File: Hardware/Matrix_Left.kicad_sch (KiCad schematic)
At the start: 125 parts, among them SW10 PG1350, SW11 PG1350, SW12 PG1350, SW13 PG1350, SW14 PG1350, SW15 PG1350, SW16 PG1350, SW17 PG1350, SW18 PG1350, SW19 PG1350, SW20 PG1350, SW21 PG1350, SW22 PG1350, SW23 PG1350, SW24 PG1350, SW25 PG1350, SW26 PG1350, SW27 PG1350, SW28 PG1350, SW29 PG1350, SW30 PG1350, SW31 PG1350, SW32 PG1350, SW33 PG1350, SW34 PG1350, SW35 PG1350, SW36 PG1350, SW37 ENCODER, SW7 PG1350, SW8 PG1350, SW9 PG1350

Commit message: MIP display and LED enable
Return of the LED enable via GPIO.
Changed the TFT display for a MPI panel. It's more expensive than an e-ink one, but the sharpness is really nice.
Need to remove the numbers row to go for a true Corne-ish layout.
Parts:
- renumbered C13 to C15, C14 to C16, C15 to C17, C16 to C18, C17 to C19, C18 to C20, C19 to C21, C20 to C22, C21 to C23, C22 to C24, C23 to C25, C24 to C26, C25 to C27, C26 to C28, C27 to C29, C28 to C30, C29 to C31, C30 to C32, C31 to C33, C32 to C34, C33 to C35, C34 to C36, C35 to C37, C36 to C38, C37 to C39, C38 to C40, C39 to C41, C40 to C42, C41 to C43, C42 to C44, C43 to C45, C44 to C46, D12 to D10, D13 to D11, D14 to D12, D15 to D13, D16 to D14, D17 to D15, D18 to D16, D19 to D17, D20 to D18, D21 to D19, D22 to D20, D23 to D21, D24 to D22, D25 to D23, D26 to D24, D27 to D25, D28 to D26, D29 to D27, D30 to D28, D31 to D29, D32 to D30, D33 to D31, D34 to D32, D35 to D33, D36 to D34, D37 to D35, D38 to D36, D39 to D37, D40 to D38, D41 to D39, D42 to D40, D43 to D41, D44 to D42, D45 to D43, D46 to D44, D47 to D45, D48 to D46, D49 to D47, D50 to D48, D51 to D49, D7 to D5, D52 to D50, D53 to D51, D54 to D52, D55 to D53, D56 to D54, D57 to D55, D58 to D56, D59 to D57, D60 to D58, D61 to D59, D8 to D6, D62 to D60, D63 to D61, D64 to D62, D65 to D63, D66 to D64, D9 to D7, D10 to D8, D11 to D9, R23 to R17, R24 to R18, SW12 to SW10, SW13 to SW11, SW14 to SW12, SW15 to SW13, SW16 to SW14, SW17 to SW15, SW18 to SW16, SW19 to SW17, SW20 to SW18, SW21 to SW19, SW22 to SW20, SW23 to SW21, SW24 to SW22, SW25 to SW23, SW26 to SW24, SW27 to SW25, SW28 to SW26, SW29 to SW27, SW30 to SW28, SW31 to SW29, SW32 to SW30, SW33 to SW31, SW34 to SW32, SW35 to SW33, SW36 to SW34, SW37 to SW35, SW7 to SW5, SW8 to SW6, SW9 to SW7, SW10 to SW8, SW11 to SW9

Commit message: Row removal and key layout
Removed the number row.
Adjusted the spacebar position and changed it to 1u.
Need to consider what to do for one of the halfs if its screen is to be removed.
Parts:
- removed C16, C19, C23, C27, C31, C35: 1u, Capacitor_SMD:C_0603_1608Metric, symbol Device:C
- removed D11, D20, D29, D38, D45, D54: 1N4148WT, Diode_SMD:D_SOD-523, symbol Diode:1N4148WT
- removed D18, D27, D36, D50, D6, D9: SK6812MINI-E, Custom_Parts:LED_SK6812MINI-E_3.2x2.8mm_P1.5mm_ReverseMount, symbol LED:SK6812MINI-E
- removed SW10, SW15, SW20, SW25, SW30, SW5: PG1350, Custom_Parts:PG1350_1.00u_PCB, symbol Switch:SW_Push
- renumbered C44 to C15, C41 to C16, C42 to C17, C40 to C18, C37 to C19, C38 to C20, C36 to C21, C33 to C22, C34 to C23, C32 to C24, C29 to C25, C30 to C26, C28 to C27, C25 to C28, C26 to C29, C24 to C30, C21 to C31, C22 to C32, C20 to C33, C17 to C34, C18 to C35, C43 to C36, C39 to C37, C15 to C38, C45 to C39, C46 to C40, D53 to D10, D12 to D11, D13 to D12, D14 to D13, D15 to D14, D51 to D15, D43 to D16, D44 to D17, D21 to D18, D22 to D19, D23 to D20, D24 to D21, D37 to D22, D34 to D23, D35 to D24, D30 to D25, D31 to D26, D32 to D27, D33 to D28, D28 to D29, D39 to D30, D40 to D31, D41 to D32, D42 to D33, D25 to D34, D26 to D35, D19 to D36, D46 to D37, D47 to D38, D48 to D39, D49 to D40, D16 to D41, D17 to D42, D10 to D43, D55 to D44, D56 to D45, D57 to D46, D58 to D47, D7 to D48, D8 to D49, D64 to D5, D63 to D50, D59 to D51, D5 to D52, D61 to D6, D62 to D7, D60 to D8, D52 to D9, SW12 to SW10, SW13 to SW11, SW14 to SW12, SW16 to SW13, SW17 to SW14, SW18 to SW15, SW19 to SW16, SW21 to SW17, SW22 to SW18, SW23 to SW19, SW24 to SW20, SW26 to SW21, SW27 to SW22, SW28 to SW23, SW29 to SW24, SW31 to SW25, SW32 to SW26, SW33 to SW27, SW34 to SW28, SW35 to SW29, SW6 to SW5, SW7 to SW6, SW8 to SW7, SW9 to SW8, SW11 to SW9
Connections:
- net ROW5_L is gone; now on net ROW4_L: D14.1 (K), D21.1 (K), D28.1 (K), D33.1 (K), D40.1 (K), D47.1 (K)
- net LED_DATA_L: now also D6.2 (DIN)
- net ROW1_L: now also D11.1 (K), D18.1 (K), D25.1 (K), D30.1 (K), D37.1 (K), D44.1 (K)
- net ROW2_L: now also D12.1 (K), D19.1 (K), D26.1 (K), D31.1 (K), D38.1 (K), D45.1 (K); no longer D11.1 (K), D18.1 (K), D25.1 (K), D30.1 (K), D37.1 (K), D44.1 (K)
- net ROW3_L: now also D13.1 (K), D20.1 (K), D27.1 (K), D32.1 (K), D39.1 (K), D46.1 (K); no longer D12.1 (K), D19.1 (K), D26.1 (K), D31.1 (K), D38.1 (K), D45.1 (K)
- net ROW4_L: no longer D13.1 (K), D20.1 (K), D27.1 (K), D32.1 (K), D39.1 (K), D46.1 (K)
- net at D51.2 (DIN): now also D48.4 (DOUT)
- net at D43.2 (DIN): now also D50.4 (DOUT); no longer D48.4 (DOUT)
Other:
- moved on the sheet: C15, C16, C17, C18, C19, C20, C21, C22, C23, C24, C25, C26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

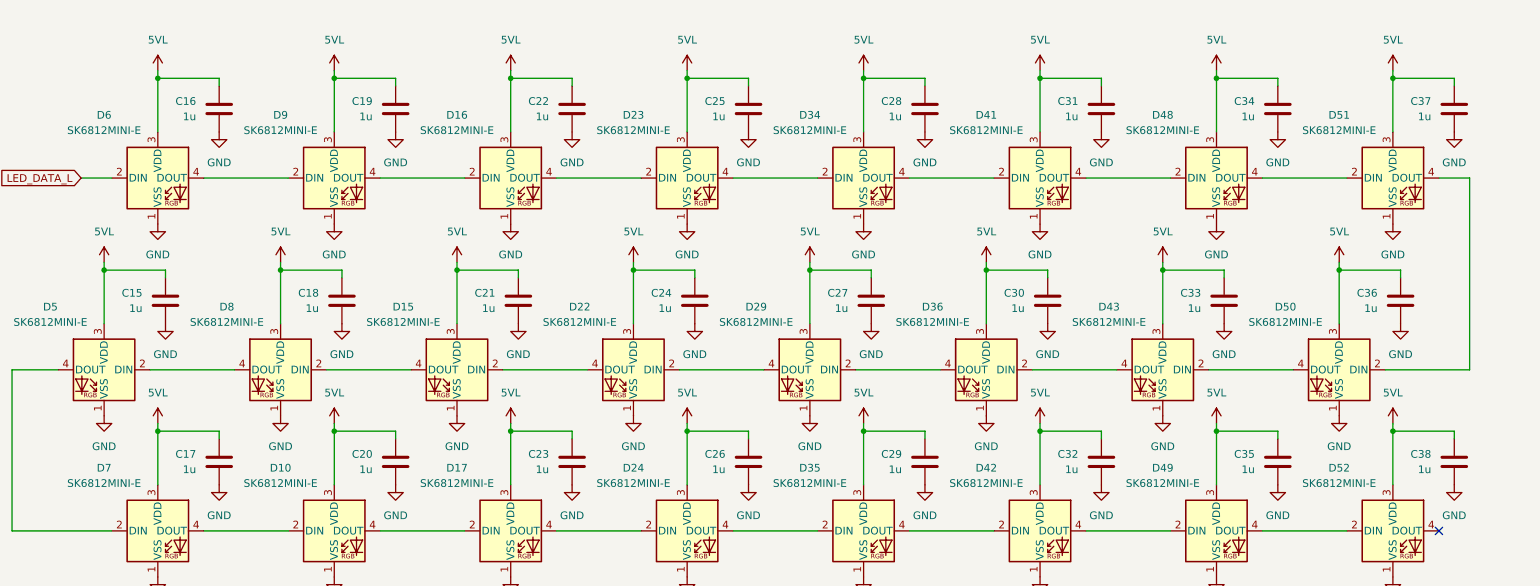
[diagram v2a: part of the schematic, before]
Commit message: Debug connector
Updated the debug connector for a custom one.
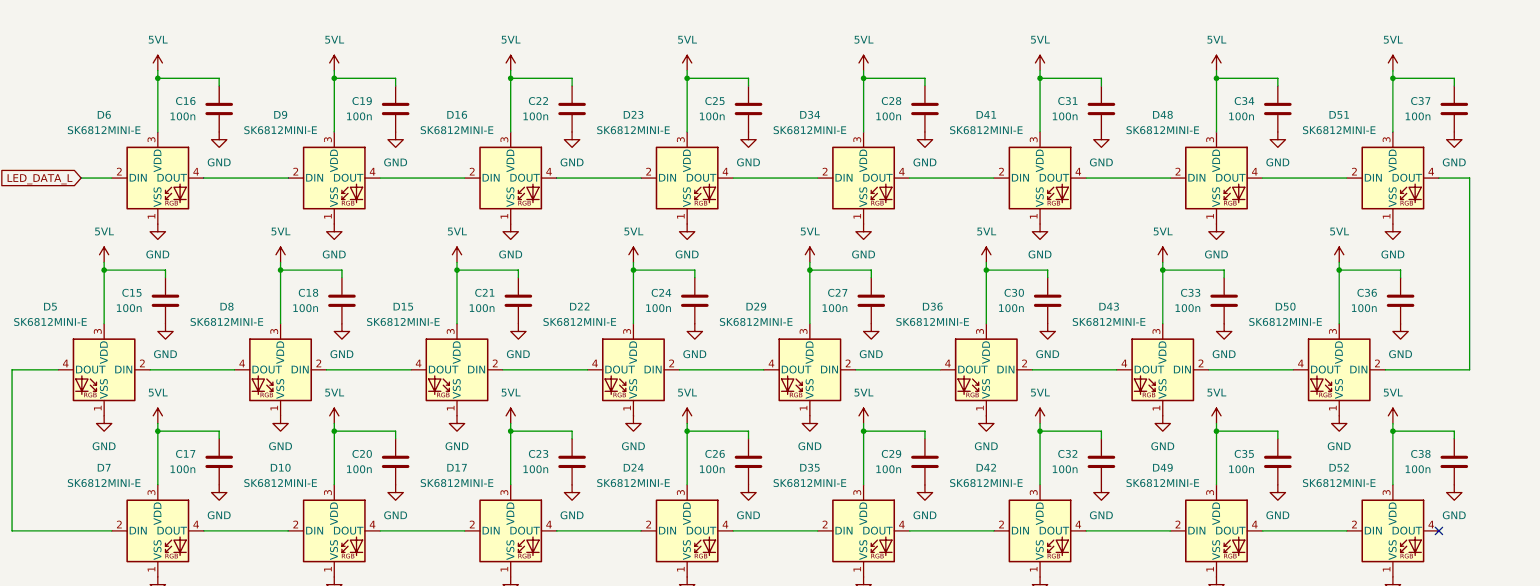
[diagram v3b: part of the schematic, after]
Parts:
- C15, C16, C17, C18, C19, C20, C21, C22, C23, C24, C25, C26, C27, C28, C29, C30, C31, C32, C33, C34, C35, C36, C37, C38: value 1u -> 100n; JLC Part C15849 -> C14663; Manufacturer Part CL10A105KB8NNNC -> CC0603KRX7R9BB104

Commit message: Board outline and routing
Enlarged the board outline by 0.5mm for proper fitment of the switch receptacles.
Updated the footprint for the switch receptacles.
Changed the JTAG connector for a custom one.
Need to review the size of the PCB area dedicated to the MCU and the screen.
Need to consider removing the additional reset button.
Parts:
- SW10, SW11, SW12, SW13, SW14, SW15, SW16, SW17, SW18, SW19, SW20, SW21, SW22, SW23, SW24, SW25, SW26, SW27, SW28, SW5, SW6, SW7, SW8, SW9: footprint Custom_Parts:PG1350_1.00u_PCB -> Custom_Parts:PG1350_1.00u_PCB_TIGHT
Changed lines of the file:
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@@
 			)
 		)
-		(property "Footprint" "Custom_Parts:PG1350_1.00u_PCB"
+		(property "Footprint" "Custom_Parts:PG1350_1.00u_PCB_TIGHT"
 			(at 139.7 57.15 0)
 			(hide yes)
@@
 			)
 		)
-		(property "Footprint" "Custom_Parts:PG1350_1.00u_PCB"
+		(property "Footprint" "Custom_Parts:PG1350_1.00u_PCB_TIGHT"
 			(at 139.7 72.39 0)
 			(hide yes)
@@
 			)
 		)
-		(property "Footprint" "Custom_Parts:PG1350_1.00u_PCB"
+		(property "Footprint" "Custom_Parts:PG1350_1.00u_PCB_TIGHT"
 			(at 166.37 102.87 0)
 			(hide yes)
@@
 			)
 		)
-		(property "Footprint" "Custom_Parts:PG1350_1.00u_PCB"
+		(property "Footprint" "Custom_Parts:PG1350_1.00u_PCB_TIGHT"
 			(at 113.03 87.63 0)
 			(hide yes)
@@
 			)
 		)
-		(property "Footprint" "Custom_Parts:PG1350_1.00u_PCB"
+		(property "Footprint" "Custom_Parts:PG1350_1.00u_PCB_TIGHT"
 			(at 219.71 102.87 0)
 			(hide yes)
@@
 			)
 		)
-		(property "Footprint" "Custom_Parts:PG1350_1.00u_PCB"
+		(property "Footprint" "Custom_Parts:PG1350_1.00u_PCB_TIGHT"
 			(at 166.37 87.63 0)
 			(hide yes)
@@
 			)
 		)
-		(property "Footprint" "Custom_Parts:PG1350_1.00u_PCB"
+		(property "Footprint" "Custom_Parts:PG1350_1.00u_PCB_TIGHT"
 			(at 193.04 87.63 0)
 			(hide yes)
@@
 			)
 		)
-		(property "Footprint" "Custom_Parts:PG1350_1.00u_PCB"
+		(property "Footprint" "Custom_Parts:PG1350_1.00u_PCB_TIGHT"
 			(at 193.04 72.39 0)
 			(hide yes)
@@
 			)
 		)
-		(property "Footprint" "Custom_Parts:PG1350_1.00u_PCB"
+		(property "Footprint" "Custom_Parts:PG1350_1.00u_PCB_TIGHT"
 			(at 113.03 57.15 0)
 			(hide yes)
@@
 			)
 		)
-		(property "Footprint" "Custom_Parts:PG1350_1.00u_PCB"
+		(property "Footprint" "Custom_Parts:PG1350_1.00u_PCB_TIGHT"
 			(at 166.37 57.15 0)
 			(hide yes)
@@
 			)
 		)
-		(property "Footprint" "Custom_Parts:PG1350_1.00u_PCB"
+		(property "Footprint" "Custom_Parts:PG1350_1.00u_PCB_TIGHT"
 			(at 193.04 102.87 0)
 			(hide yes)
@@
 			)
 		)
-		(property "Footprint" "Custom_Parts:PG1350_1.00u_PCB"
+		(property "Footprint" "Custom_Parts:PG1350_1.00u_PCB_TIGHT"
 			(at 139.7 87.63 0)
 			(hide yes)
@@
 			)
 		)
-		(property "Footprint" "Custom_Parts:PG1350_1.00u_PCB"
+		(property "Footprint" "Custom_Parts:PG1350_1.00u_PCB_TIGHT"
 			(at 86.36 57.15 0)
 			(hide yes)
@@
 			)
 		)
-		(property "Footprint" "Custom_Parts:PG1350_1.00u_PCB"
+		(property "Footprint" "Custom_Parts:PG1350_1.00u_PCB_TIGHT"
 			(at 166.37 72.39 0)
 			(hide yes)
@@
 			)
 		)
-		(property "Footprint" "Custom_Parts:PG1350_1.00u_PCB"
+		(property "Footprint" "Custom_Parts:PG1350_1.00u_PCB_TIGHT"
 			(at 86.36 72.39 0)
 			(hide yes)
@@
 			)
 		)
-		(property "Footprint" "Custom_Parts:PG1350_1.00u_PCB"
+		(property "Footprint" "Custom_Parts:PG1350_1.00u_PCB_TIGHT"
 			(at 139.7 102.87 0)
 			(hide yes)
@@
 			)
 		)
-		(property "Footprint" "Custom_Parts:PG1350_1.00u_PCB"
+		(property "Footprint" "Custom_Parts:PG1350_1.00u_PCB_TIGHT"
 			(at 113.03 102.87 0)
 			(hide yes)
@@
 			)
 		)
-		(property "Footprint" "Custom_Parts:PG1350_1.00u_PCB"
+		(property "Footprint" "Custom_Parts:PG1350_1.00u_PCB_TIGHT"
 			(at 219.71 57.15 0)
 			(hide yes)
@@
 			)
 		)
-		(property "Footprint" "Custom_Parts:PG1350_1.00u_PCB"
+		(property "Footprint" "Custom_Parts:PG1350_1.00u_PCB_TIGHT"
 			(at 219.71 87.63 0)
 			(hide yes)
@@
 			)
 		)
-		(property "Footprint" "Custom_Parts:PG1350_1.00u_PCB"
+		(property "Footprint" "Custom_Parts:PG1350_1.00u_PCB_TIGHT"
 			(at 86.36 102.87 0)
 			(hide yes)
@@
 			)
 		)
-		(property "Footprint" "Custom_Parts:PG1350_1.00u_PCB"
+		(property "Footprint" "Custom_Parts:PG1350_1.00u_PCB_TIGHT"
 			(at 193.04 57.15 0)
 			(hide yes)
@@
 			)
 		)
-		(property "Footprint" "Custom_Parts:PG1350_1.00u_PCB"
+		(property "Footprint" "Custom_Parts:PG1350_1.00u_PCB_TIGHT"
 			(at 219.71 72.39 0)
 			(hide yes)
@@
 			)
 		)
-		(property "Footprint" "Custom_Parts:PG1350_1.00u_PCB"
+		(property "Footprint" "Custom_Parts:PG1350_1.00u_PCB_TIGHT"
 			(at 86.36 87.63 0)
 			(hide yes)
@@
 			)
 		)
-		(property "Footprint" "Custom_Parts:PG1350_1.00u_PCB"
+		(property "Footprint" "Custom_Parts:PG1350_1.00u_PCB_TIGHT"
 			(at 113.03 72.39 0)
 			(hide yes)

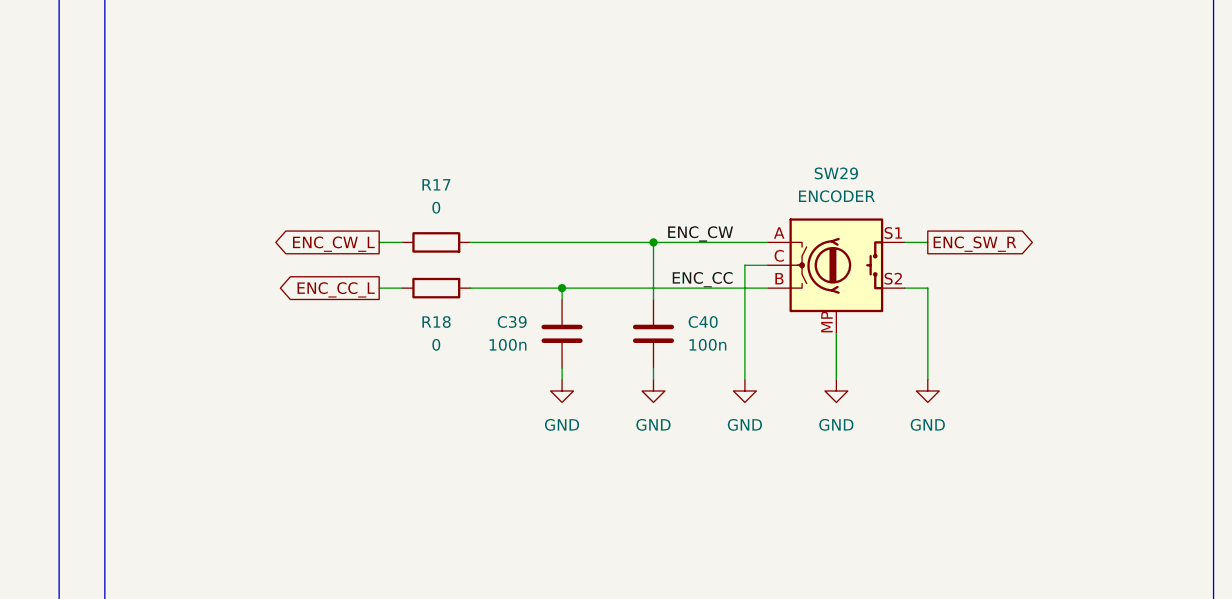
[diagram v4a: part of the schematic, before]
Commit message: Matrix routing and data lines
Routed some of the lines for the switch matrix.
Routed the singal lines for the MIP display.
Need to check clearenaces and spacing between the SPI lines.
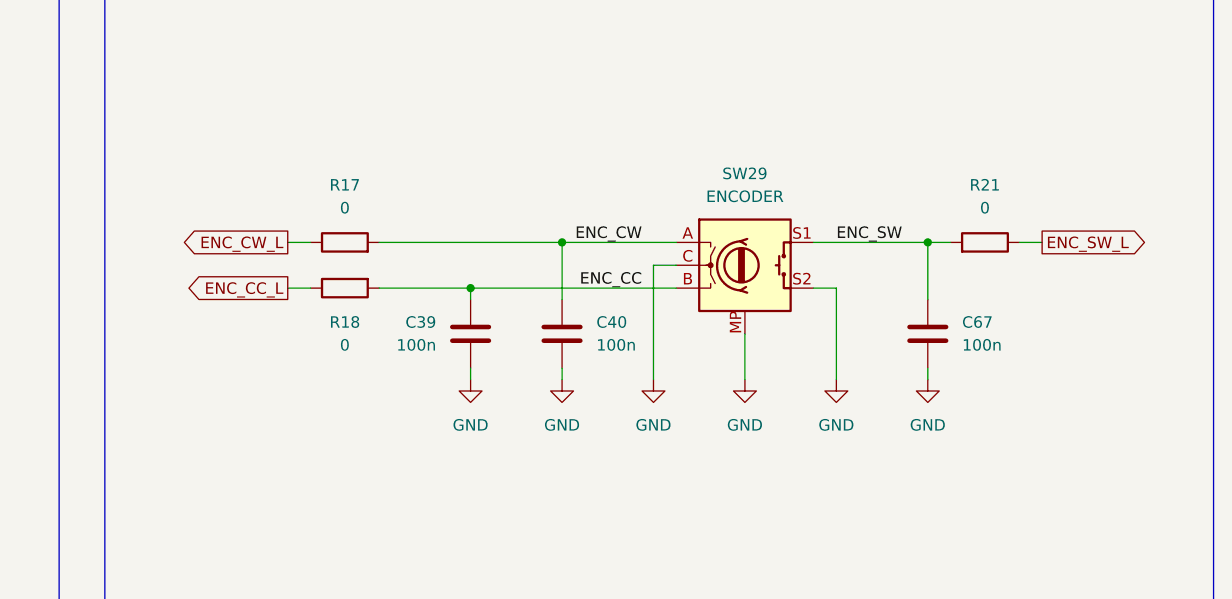
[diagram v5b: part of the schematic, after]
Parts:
- added C67: 100n, Capacitor_SMD:C_0603_1608Metric, symbol Device:C
- added R21: 0, Resistor_SMD:R_0603_1608Metric, symbol Device:R
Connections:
- net GND: now also C67.2
- net ENC_SW_R renamed ENC_SW
- net ENC_SW: now also C67.1, R21.2
- new net ENC_SW_L: R21.1
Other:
- moved on the sheet: C39, C40, R17, R18, SW29
